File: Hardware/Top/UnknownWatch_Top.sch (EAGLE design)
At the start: 49 parts, among them U2 NRF52832_MODULE_MDBT42, U4 PCF8523

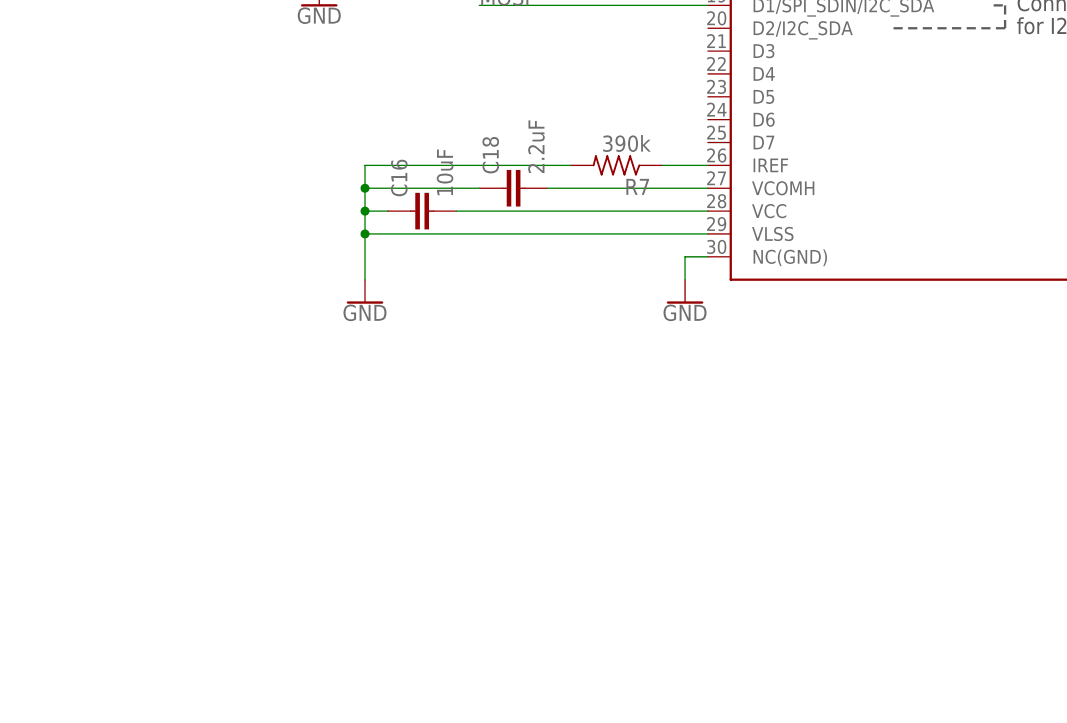
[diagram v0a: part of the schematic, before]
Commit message: Adde Buttons
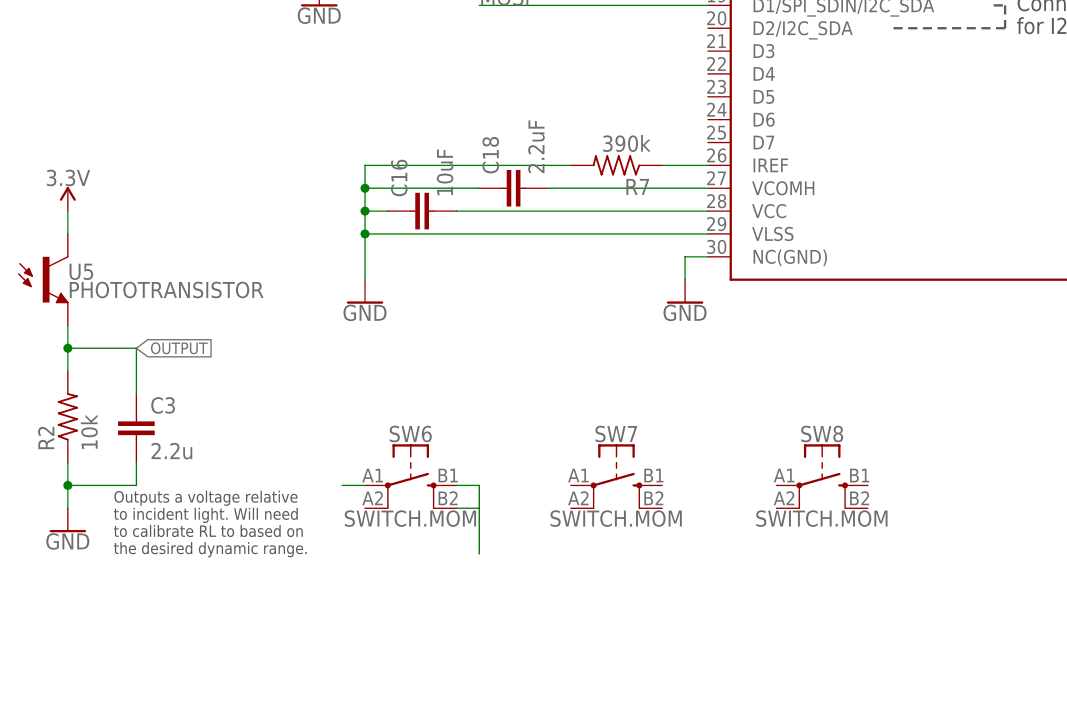
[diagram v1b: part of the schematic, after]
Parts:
- added C3: 2.2u, LinnesLab-Passives:CAPACITOR0603
- added R2: 10k, LinnesLab-Passives:RESISTOR0603
- added SW6, SW7, SW8: SWITCH.MOM, LinnesLab-Switches:SWITCH.MOM
- added U5: PHOTOTRANSISTOR, LinnesLab-Sensors:PHOTOTRANSISTOR
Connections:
- new net N$16: SW6.3, SW6.4
- new net N$18: SW6.1
- new net OUTPUT: C3.1, R2.2, U5.E
- net 3.3V: now also U5.C
- net GND: now also C3.2, R2.1
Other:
- note added: "Outputs a voltage relative to incident light. Will need to calibrate RL to based on the desired dynamic range."
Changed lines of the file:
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@@
 <attribute name="MFN_MANUFACTURER" value="NXP USA Inc."/>
 </part>
+<part name="U5" library="LinnesLab-Sensors" deviceset="PHOTOTRANSISTOR" device="" package3d_urn="urn:adsk.eagle:package:17881375/3"/>
+<part name="R2" library="LinnesLab-Passives" deviceset="RESISTOR" device="0603" package3d_urn="urn:adsk.eagle:package:15661944/2" value="10k"/>
+<part name="C3" library="LinnesLab-Passives" deviceset="CAPACITOR" device="0603" package3d_urn="urn:adsk.eagle:package:15661989/2" value="2.2u"/>
+<part name="GND3" library="LinnesLab-Symbols" deviceset="GND" device=""/>
+<part name="SUPPLY7" library="LinnesLab-Symbols" deviceset="3.3V" device=""/>
+<part name="SW6" library="LinnesLab-Switches" deviceset="SWITCH.MOM" device=""/>
+<part name="SW7" library="LinnesLab-Switches" deviceset="SWITCH.MOM" device=""/>
+<part name="SW8" library="LinnesLab-Switches" deviceset="SWITCH.MOM" device=""/>
 </parts>
 <sheets>
@@
 battery
 if desired</text>
+<text x="-127" y="25.4" size="1.27" layer="97">Outputs a voltage relative
+to incident light. Will need
+to calibrate RL to based on
+the desired dynamic range.</text>
 </plain>
 <instances>
@@
 <attribute name="MFN" x="-78.74" y="182.88" size="1.27" layer="96" display="off"/>
 <attribute name="MFN_MANUFACTURER" x="-78.74" y="182.88" size="1.27" layer="96" display="off"/>
+</instance>
+<instance part="U5" gate="G$1" x="-134.62" y="55.88" smashed="yes">
+<attribute name="NAME" x="-132.08" y="55.88" size="1.778" layer="95" font="vector"/>
+<attribute name="VALUE" x="-132.08" y="55.626" size="1.778" layer="96" font="vector" align="top-left"/>
+</instance>
+<instance part="R2" gate="G$1" x="-132.08" y="40.64" smashed="yes" rot="R90">
+<attribute name="NAME" x="-133.5786" y="36.83" size="1.778" layer="95" rot="R90"/>
+<attribute name="VALUE" x="-128.778" y="36.83" size="1.778" layer="96" rot="R90"/>
+</instance>
+<instance part="C3" gate="G$1" x="-124.46" y="38.1" smashed="yes">
+<attribute name="NAME" x="-122.936" y="41.021" size="1.778" layer="95"/>
+<attribute name="VALUE" x="-122.936" y="35.941" size="1.778" layer="96"/>
+</instance>
+<instance part="GND3" gate="G$1" x="-132.08" y="27.94" smashed="yes">
+<attribute name="VALUE" x="-132.08" y="27.686" size="1.778" layer="96" align="top-center"/>
+</instance>
+<instance part="SUPPLY7" gate="G$1" x="-132.08" y="63.5" smashed="yes">
+<attribute name="VALUE" x="-132.08" y="66.294" size="1.778" layer="96" align="bottom-center"/>
+</instance>
+<instance part="SW6" gate="G$1" x="-93.98" y="33.02" smashed="yes">
+<attribute name="NAME" x="-93.98" y="37.846" size="1.778" layer="95" font="vector" align="bottom-center"/>
+<attribute name="VALUE" x="-93.98" y="30.226" size="1.778" layer="96" font="vector" align="top-center"/>
+</instance>
+<instance part="SW7" gate="G$1" x="-71.12" y="33.02" smashed="yes">
+<attribute name="NAME" x="-71.12" y="37.846" size="1.778" layer="95" font="vector" align="bottom-center"/>
+<attribute name="VALUE" x="-71.12" y="30.226" size="1.778" layer="96" font="vector" align="top-center"/>
+</instance>
+<instance part="SW8" gate="G$1" x="-48.26" y="33.02" smashed="yes">
+<attribute name="NAME" x="-48.26" y="37.846" size="1.778" layer="95" font="vector" align="bottom-center"/>
+<attribute name="VALUE" x="-48.26" y="30.226" size="1.778" layer="96" font="vector" align="top-center"/>
 </instance>
 </instances>
@@
 <pinref part="C2" gate="G$1" pin="2"/>
 </segment>
+<segment>
+<pinref part="C3" gate="G$1" pin="2"/>
+<wire x1="-124.46" y1="35.56" x2="-124.46" y2="33.02" width="0.1524" layer="91"/>
+<wire x1="-124.46" y1="33.02" x2="-132.08" y2="33.02" width="0.1524" layer="91"/>
+<pinref part="R2" gate="G$1" pin="1"/>
+<wire x1="-132.08" y1="33.02" x2="-132.08" y2="35.56" width="0.1524" layer="91"/>
+<pinref part="GND3" gate="G$1" pin="GND"/>
+<wire x1="-132.08" y1="30.48" x2="-132.08" y2="33.02" width="0.1524" layer="91"/>
+<junction x="-132.08" y="33.02"/>
+</segment>
 </net>
 <net name="SWDIO" class="0">
@@
 <pinref part="SUPPLY19" gate="G$1" pin="3.3V"/>
 <wire x1="-45.72" y1="195.58" x2="-45.72" y2="193.04" width="0.1524" layer="91"/>
+</segment>
+<segment>
+<pinref part="U5" gate="G$1" pin="C"/>
+<wire x1="-132.08" y1="60.96" x2="-132.08" y2="63.5" width="0.1524" layer="91"/>
+<pinref part="SUPPLY7" gate="G$1" pin="3.3V"/>
 </segment>
 </net>
@@
 </segment>
 </net>
+<net name="OUTPUT" class="0">
+<segment>
+<pinref part="U5" gate="G$1" pin="E"/>
+<pinref part="R2" gate="G$1" pin="2"/>
+<wire x1="-132.08" y1="45.72" x2="-132.08" y2="48.26" width="0.1524" layer="91"/>
+<pinref part="C3" gate="G$1" pin="1"/>
+<wire x1="-132.08" y1="48.26" x2="-132.08" y2="50.8" width="0.1524" layer="91"/>
+<wire x1="-124.46" y1="43.18" x2="-124.46" y2="48.26" width="0.1524" layer="91"/>
+<wire x1="-124.46" y1="48.26" x2="-132.08" y2="48.26" width="0.1524" layer="91"/>
+<junction x="-132.08" y="48.26"/>
+<label x="-124.46" y="48.26" size="1.27" layer="95" xref="yes"/>
+</segment>
+</net>
+<net name="N$16" class="0">
+<segment>
+<pinref part="SW6" gate="G$1" pin="3"/>
+<wire x1="-88.9" y1="33.02" x2="-86.36" y2="33.02" width="0.1524" layer="91"/>
+<wire x1="-86.36" y1="33.02" x2="-86.36" y2="30.48" width="0.1524" layer="91"/>
+<pinref part="SW6" gate="G$1" pin="4"/>
+<wire x1="-86.36" y1="25.4" x2="-86.36" y2="30.48" width="0.1524" layer="91"/>
+<wire x1="-86.36" y1="30.48" x2="-88.9" y2="30.48" width="0.1524" layer="91"/>
+</segment>
+</net>
+<net name="N$18" class="0">
+<segment>
+<pinref part="SW6" gate="G$1" pin="1"/>
+<wire x1="-99.06" y1="33.02" x2="-101.6" y2="33.02" width="0.1524" layer="91"/>
+</segment>
+</net>

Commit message: Added segmentation and labels to schematic
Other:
- note added: "Ambient Light Sensor"
- note added: "Buttons"
- note added: "Cortex Debugger/ Programmer"
- note added: "Power Management"
- note added: "RTC"
- note added: "Real-Time Clock"
- note added: "SD Card"
- note added: "nRF52832 Module"
- moved on the sheet: C10, C11, C12, C13, C14, C15, C16, C17, C18, C19, C2, C20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
